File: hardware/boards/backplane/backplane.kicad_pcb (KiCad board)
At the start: 2 copper layers, 44 parts, among them J10 I2C_IN, J11 I2C_OUT, J12 LED_EXT_OUT, J13 FAN_3PIN, J2 SLOT_1, J3 SLOT_2, J4 SLOT_3, J5 SLOT_4, J6 SLOT_5, J7 SLOT_6, J8 LED_EXT_IN, Q1 Q_PMOS_GSD, Q2 Q_NPN_BEC, U1 TCA9548APWR, U2 WT32-ETH01

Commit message: Small tweaks to PCB/Schematic + 3d models
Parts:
- added D10: LOW_CAP_TVS, Diode_SMD:D_SOD-523, F.Cu at (65.5, 18.1)
- added D12: LOW_CAP_TVS, Diode_SMD:D_SOD-523, F.Cu at (69.1, 13.2)
- added D14: LOW_CAP_TVS, Diode_SMD:D_SOD-523, F.Cu at (69.1, 18.1)
- added D16: LOW_CAP_TVS, Diode_SMD:D_SOD-523, F.Cu at (72.7, 13.2)
- added D18: LOW_CAP_TVS, Diode_SMD:D_SOD-523, F.Cu at (72.7, 18.1)
- added D8: LOW_CAP_TVS, Diode_SMD:D_SOD-523, F.Cu at (65.5, 13.2)
- added H1: MountingHole_Pad, MountingHole:MountingHole_3.2mm_M3_Pad_Via, F.Cu at (-3.90, 0.50)
- added H2: MountingHole_Pad, MountingHole:MountingHole_3.2mm_M3_Pad_Via, F.Cu at (3.48, 11.4)
- added H3: MountingHole_Pad, MountingHole:MountingHole_3.2mm_M3_Pad_Via, F.Cu at (3.48, 19.4)
- added H4: MountingHole_Pad, MountingHole:MountingHole_3.2mm_M3_Pad_Via, F.Cu at (3.48, 27.3)
- added R11: 47R, Resistor_SMD:R_0603_1608Metric, F.Cu at (73.7, 3.27)
- added R13: 47R, Resistor_SMD:R_0603_1608Metric, F.Cu at (73.7, 8.29)
- added R3: 47R, Resistor_SMD:R_0603_1608Metric, F.Cu at (65.7, 3.27)
- added R5: 47R, Resistor_SMD:R_0603_1608Metric, F.Cu at (65.7, 8.29)
- added R7: 47R, Resistor_SMD:R_0603_1608Metric, F.Cu at (69.7, 3.27)
- added R9: 47R, Resistor_SMD:R_0603_1608Metric, F.Cu at (69.7, 8.29)
- J2: value SLOT_1 -> SLOT_4
- J3: value SLOT_2 -> SLOT_1
- J4: value SLOT_3 -> SLOT_2
- J5: value SLOT_4 -> SLOT_5
- J6: value SLOT_5 -> SLOT_6
- J7: value SLOT_6 -> SLOT_3
- moved J12 217.8 mm to (44.1, 14.0)
- moved J11 215.1 mm to (44.1, 1.79)
- moved D1 173.9 mm to (33.1, 2.81)
- moved D2 173.9 mm to (33.1, 9.43)
- moved D3 173.9 mm to (33.1, 16.1)
- moved D4 173.9 mm to (33.1, 22.7)
- moved D5 173.9 mm to (33.1, 29.3)
- moved D6 173.9 mm to (33.1, 35.9)
- moved J2 137.1 mm to (56.0, 2.62)
- moved J3 137.1 mm to (56.0, 8.88)
- moved J4 137.1 mm to (56.0, 15.1)
- moved J5 137.1 mm to (56.0, 21.4)
- moved J6 137.1 mm to (56.0, 27.6)
- moved J7 137.1 mm to (56.0, 33.9)
- moved R12 121.3 mm to (73.7, 5.78)
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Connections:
- J2 pad 3: SCL_SLOT_1_CONN -> Net-(D16-A1)
- J3 pad 3: SCL_SLOT_2_CONN -> Net-(D8-A1)
- J4 pad 3: SCL_SLOT_3_CONN -> Net-(D14-A1)
- J4 pad 4: Net-(D11-A1) -> Net-(D10-A1)
- J5 pad 3: SCL_SLOT_4_CONN -> Net-(D17-A1)
- J5 pad 4: Net-(D13-A1) -> Net-(D11-A1)
- J6 pad 3: SCL_SLOT_5_CONN -> Net-(D18-A1)
- J6 pad 4: Net-(D15-A1) -> Net-(D12-A1)
- J7 pad 3: SCL_SLOT_6_CONN -> Net-(D15-A1)
- J7 pad 4: Net-(D17-A1) -> Net-(D13-A1)
- R10 pad 1: SDA_SLOT_5 -> SCL_SLOT_3_CONN
- R12 pad 1: SDA_SLOT_6 -> SCL_SLOT_5_CONN
- R2 pad 1: SDA_SLOT_1 -> SDA_SLOT_4
- R4 pad 1: SDA_SLOT_2 -> SDA_SLOT_1
- R6 pad 1: SDA_SLOT_3 -> SDA_SLOT_5
- R8 pad 1: SDA_SLOT_4 -> SDA_SLOT_3

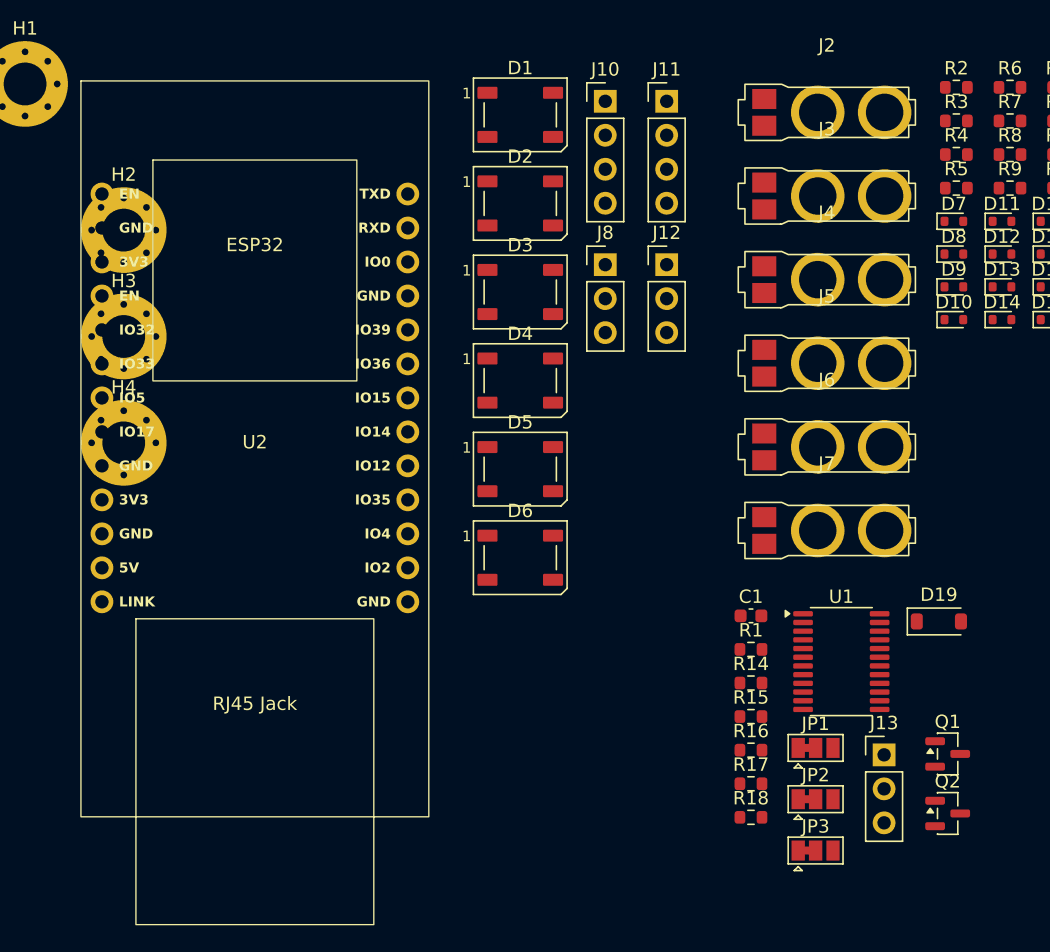
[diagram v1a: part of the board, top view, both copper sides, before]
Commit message: Split controller hardware from backplane
Add the central controller KiCad project for the WT32 and fan circuit, retain the I2C mux on the backplane, and update the system/interface documentation. Use C7519 arrays for interim slot I2C protection and record assembly-part alternatives.
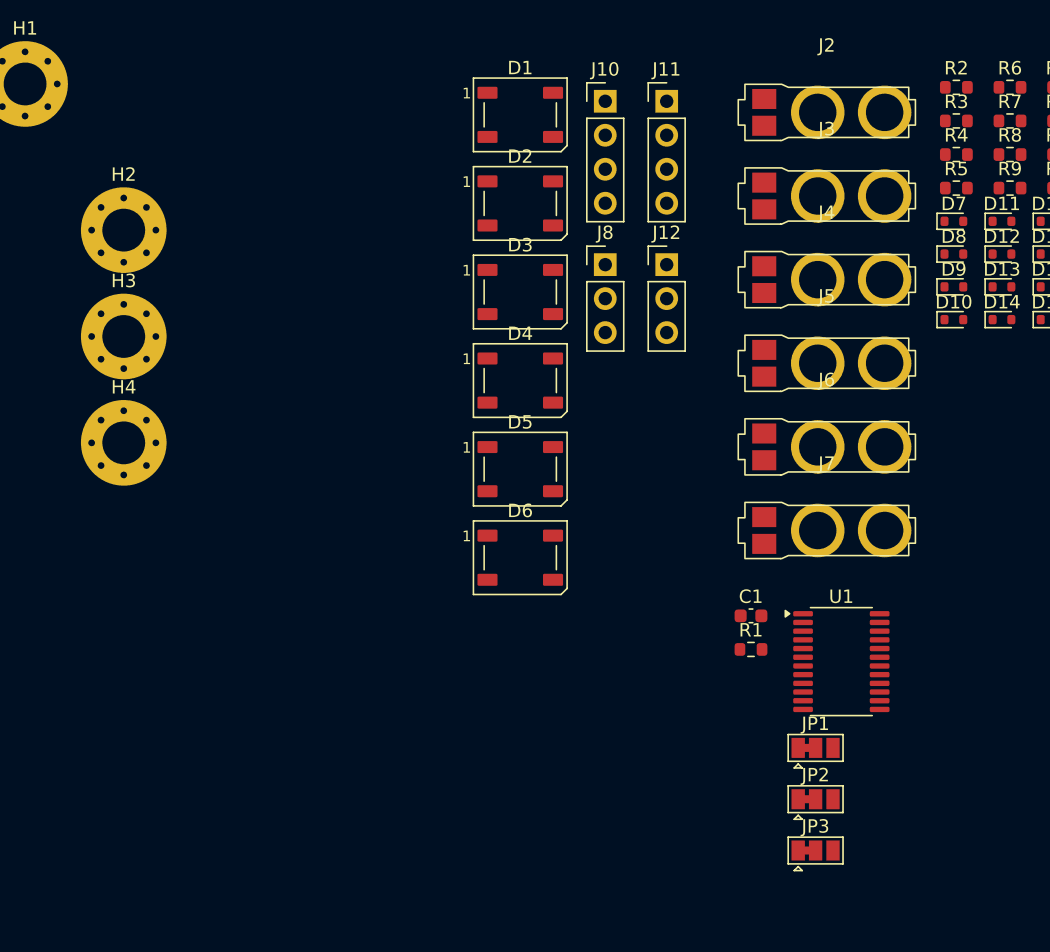
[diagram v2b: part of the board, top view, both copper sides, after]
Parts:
- removed D19: D_Schottky, Diode_SMD:D_SOD-123
- removed J13: FAN_3PIN, Connector_PinHeader_2.54mm:PinHeader_1x03_P2.54mm_Vertical
- removed Q1: Q_PMOS_GSD, Package_TO_SOT_SMD:SOT-23
- removed Q2: Q_NPN_BEC, Package_TO_SOT_SMD:SOT-23
- removed R14, R16: 100k, Resistor_SMD:R_0603_1608Metric
- removed R15: 4.7k, Resistor_SMD:R_0603_1608Metric
- removed R17: 10k, Resistor_SMD:R_0603_1608Metric
- removed R18: 1k, Resistor_SMD:R_0603_1608Metric
- removed U2: WT32-ETH01, WT32-ETH01:WT32-ETH01
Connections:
- net /I2C and Fan/TCA9548A_A0 renamed /I2C Mux/TCA9548A_A0
- net /I2C and Fan/TCA9548A_A1 renamed /I2C Mux/TCA9548A_A1
- net /I2C and Fan/TCA9548A_A2 renamed /I2C Mux/TCA9548A_A2
- net Net-(D1-DIN) renamed /Slots and LEDs/LED_DATA_IN
- J10 pad 4: +5V -> +3V3
- J11 pad 4: +5V -> +3V3

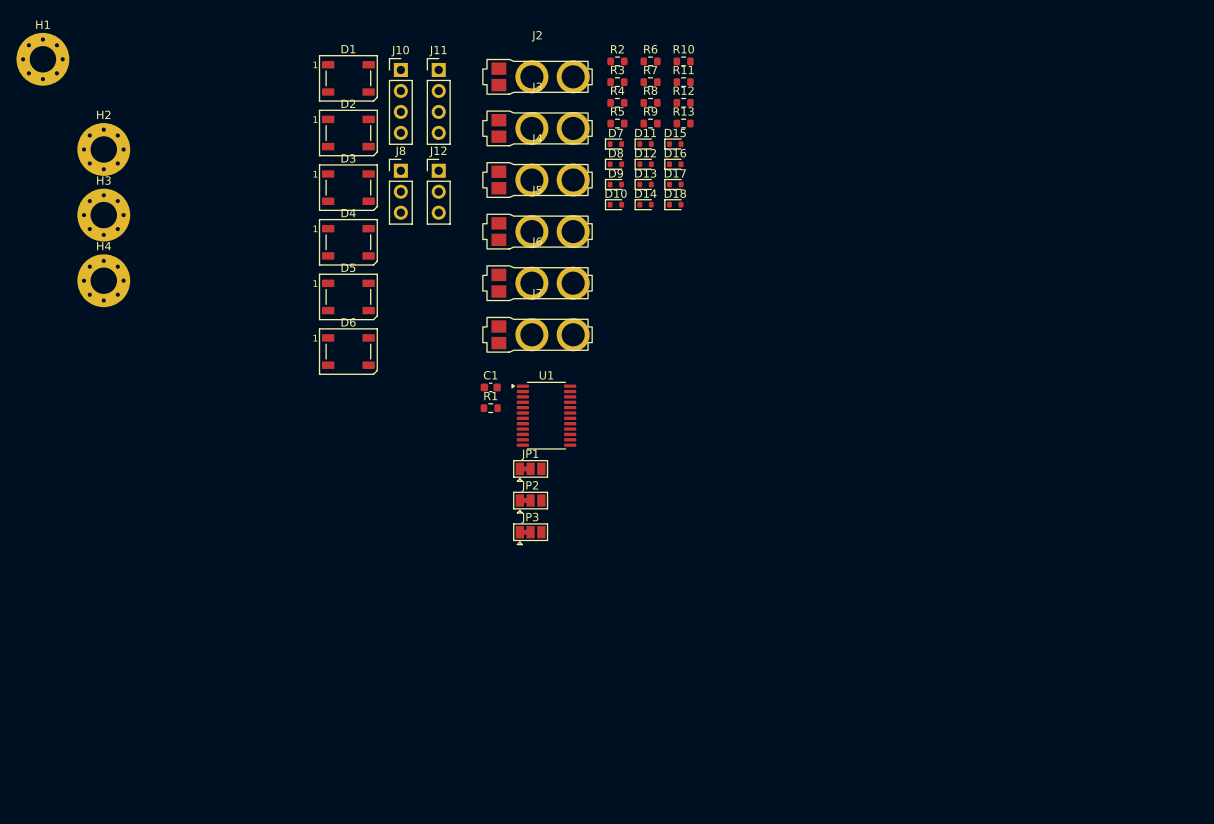
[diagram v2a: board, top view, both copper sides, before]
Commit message: Add adjustable DC-DC module to backplane
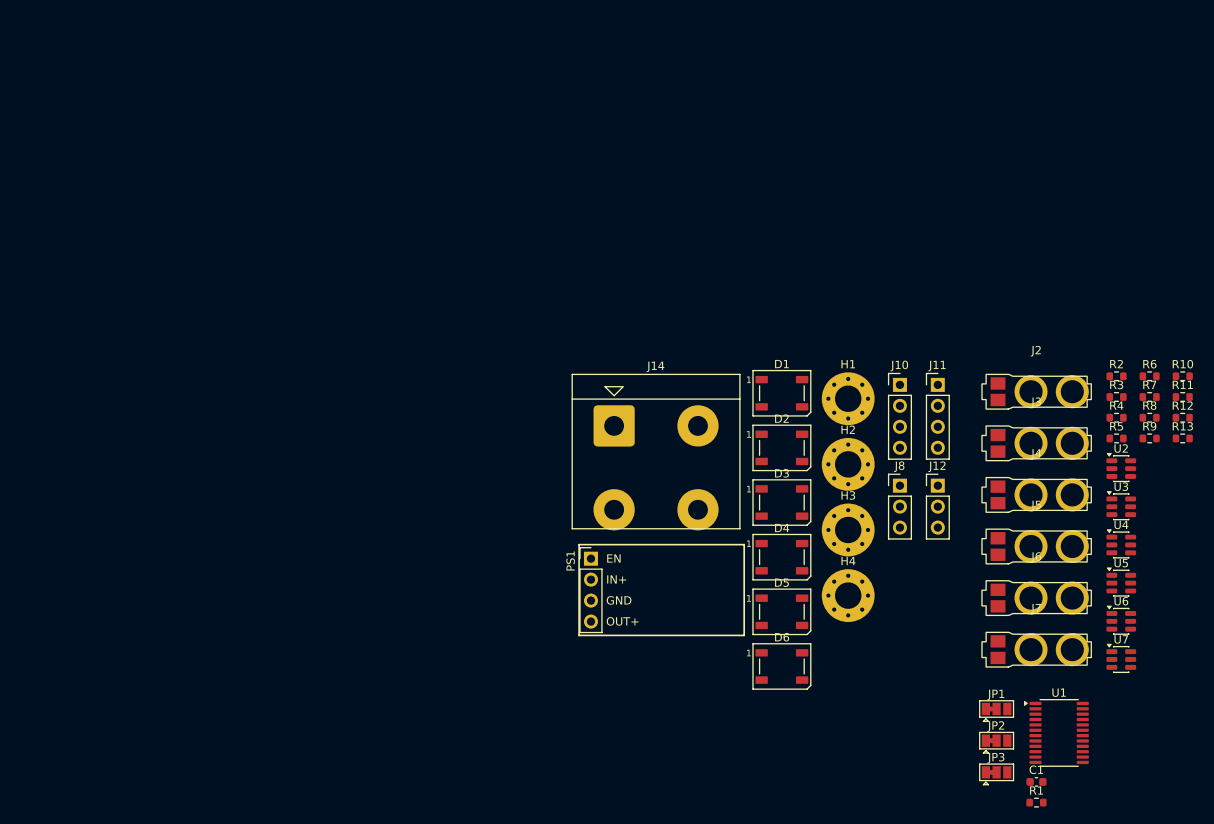
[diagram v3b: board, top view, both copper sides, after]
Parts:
- removed D10, D11, D12, D13, D14, D15, D16, D17, D18, D7, D8, D9: LOW_CAP_TVS, Diode_SMD:D_SOD-523
- added J14: DC_IN, mini-rack-power:DEGSON_DG135T-10.16-02P, F.Cu at (65.3, 44.9)
- added PS1: Adjustable_DC2DC, mini-rack-power:Adjustable_DC2DC, F.Cu at (62.5, 61.0)
- added U2: USBLC6-2SC6, Package_TO_SOT_SMD:SOT-23-6, F.Cu at (126.7, 50.1)
- added U3: USBLC6-2SC6, Package_TO_SOT_SMD:SOT-23-6, F.Cu at (126.7, 54.7)
- added U4: USBLC6-2SC6, Package_TO_SOT_SMD:SOT-23-6, F.Cu at (126.7, 59.3)
- added U5: USBLC6-2SC6, Package_TO_SOT_SMD:SOT-23-6, F.Cu at (126.7, 64.0)
- added U6: USBLC6-2SC6, Package_TO_SOT_SMD:SOT-23-6, F.Cu at (126.7, 68.6)
- added U7: USBLC6-2SC6, Package_TO_SOT_SMD:SOT-23-6, F.Cu at (126.7, 73.2)
- moved H1 105.9 mm to (93.7, 41.6)
- moved H2 97.9 mm to (93.7, 49.6)
- moved H3 97.9 mm to (93.7, 57.5)
- moved H4 97.9 mm to (93.7, 65.5)
- moved R1 81.6 mm to (116.5, 90.6)
- moved C1 81.6 mm to (116.5, 88.0)
- moved U1 73.0 mm to (119.2, 82.1)
- moved J10 71.5 mm to (99.9, 39.9)
- moved J6 71.5 mm to (116.5, 65.8)
- moved J7 71.5 mm to (116.5, 72.0)
- moved J8 71.5 mm to (99.9, 52.2)
- moved R10 71.5 mm to (134.2, 38.9)
- moved R11 71.5 mm to (134.2, 41.4)
- moved R12 71.5 mm to (134.2, 43.9)
- moved R13 71.5 mm to (134.2, 46.4)
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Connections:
- J2 pad 3: Net-(D16-A1) -> Net-(J2-Pin_3)
- J2 pad 4: Net-(D7-A1) -> Net-(J2-Pin_4)
- J3 pad 3: Net-(D8-A1) -> Net-(J3-Pin_3)
- J3 pad 4: Net-(D9-A1) -> Net-(J3-Pin_4)
- J4 pad 3: Net-(D14-A1) -> Net-(J4-Pin_3)
- J4 pad 4: Net-(D10-A1) -> Net-(J4-Pin_4)
- J5 pad 3: Net-(D17-A1) -> Net-(J5-Pin_3)
- J5 pad 4: Net-(D11-A1) -> Net-(J5-Pin_4)
- J6 pad 3: Net-(D18-A1) -> Net-(J6-Pin_3)
- J6 pad 4: Net-(D12-A1) -> Net-(J6-Pin_4)
- J7 pad 3: Net-(D15-A1) -> Net-(J7-Pin_3)
- J7 pad 4: Net-(D13-A1) -> Net-(J7-Pin_4)
- R10 pad 1: SCL_SLOT_3_CONN -> SCL_SLOT_3
- R10 pad 2: Net-(D15-A1) -> Net-(R10-Pad2)
- R11 pad 1: SCL_SLOT_4_CONN -> SCL_SLOT_4
- R11 pad 2: Net-(D16-A1) -> Net-(R11-Pad2)
- R12 pad 1: SCL_SLOT_5_CONN -> SCL_SLOT_5
- R12 pad 2: Net-(D17-A1) -> Net-(R12-Pad2)
- R13 pad 1: SCL_SLOT_6_CONN -> SCL_SLOT_6
- R13 pad 2: Net-(D18-A1) -> Net-(R13-Pad2)
- R2 pad 2: Net-(D7-A1) -> Net-(R2-Pad2)
- R3 pad 1: SCL_SLOT_1_CONN -> SCL_SLOT_1
- R3 pad 2: Net-(D8-A1) -> Net-(R3-Pad2)
- R4 pad 2: Net-(D9-A1) -> Net-(R4-Pad2)
- R5 pad 2: Net-(D10-A1) -> Net-(R5-Pad2)
- R6 pad 2: Net-(D11-A1) -> Net-(R6-Pad2)
- R7 pad 2: Net-(D12-A1) -> Net-(R7-Pad2)
- R8 pad 2: Net-(D13-A1) -> Net-(R8-Pad2)
- R9 pad 1: SCL_SLOT_2_CONN -> SCL_SLOT_2
- R9 pad 2: Net-(D14-A1) -> Net-(R9-Pad2)

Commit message: Save initial backplane placement work
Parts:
- added J1: SPARE_I2C, Connector_PinHeader_2.54mm:PinHeader_1x04_P2.54mm_Vertical, F.Cu at (-26.1, 46.2)
- moved C1 136.8 mm to (-16.1, 54.5)
- moved JP1 136.8 mm to (-20.9, 45.7)
- moved JP2 136.8 mm to (-20.9, 49.5)
- moved JP3 136.8 mm to (-20.9, 53.4)
- moved R1 136.8 mm to (-16.1, 57.0)
- moved U1 136.8 mm to (-13.4, 48.6)
- moved H1 129.1 mm to (-32.0, 71.2)
- moved H2 129.1 mm to (-32.0, 79.2)
- moved H3 129.1 mm to (-32.0, 87.1)
- moved H4 129.1 mm to (-32.0, 95.0)
- moved J10 121.1 mm to (-18.8, 16.5)
- moved J11 121.1 mm to (-14.2, 16.5)
- moved J12 121.1 mm to (-14.2, 28.7)
- moved J8 121.1 mm to (-18.8, 28.7)
- moved PS1 92.9 mm to (-25.5, 90.7)
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
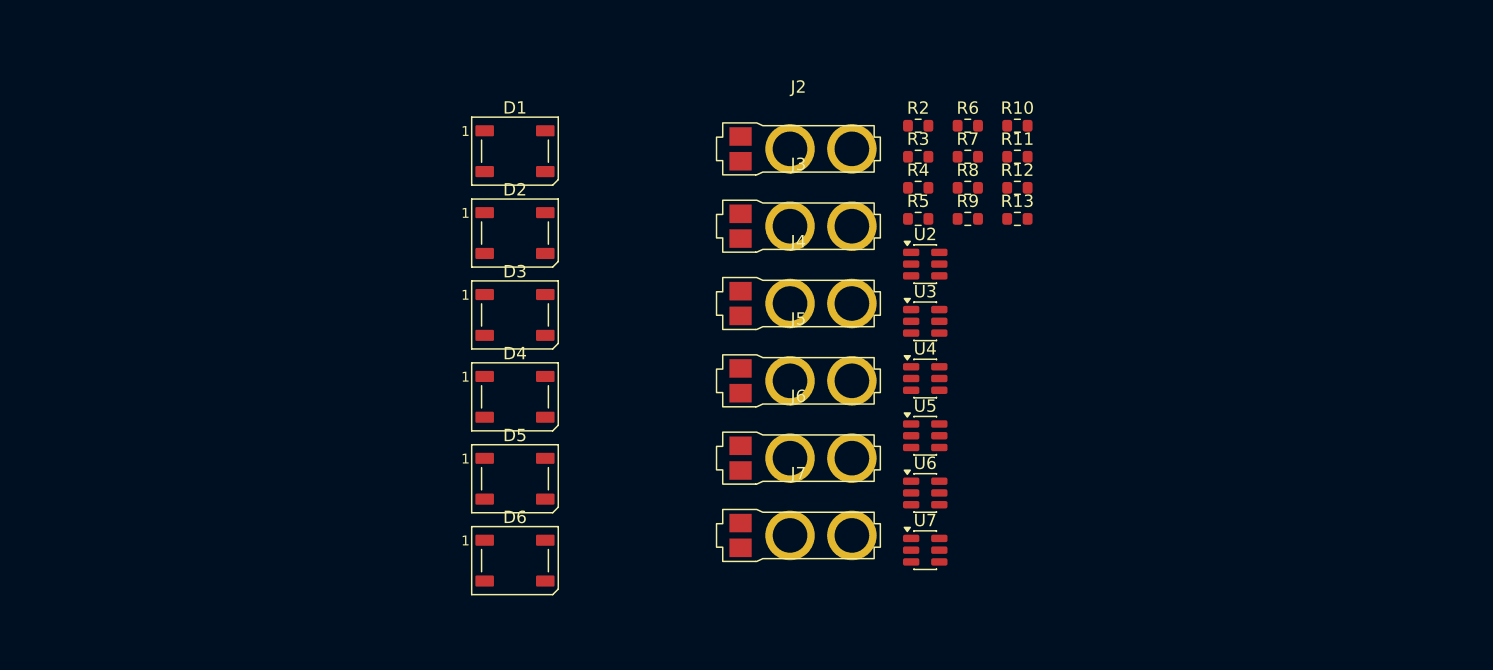
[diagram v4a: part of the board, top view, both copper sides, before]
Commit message: Arrange backplane slot connector groups
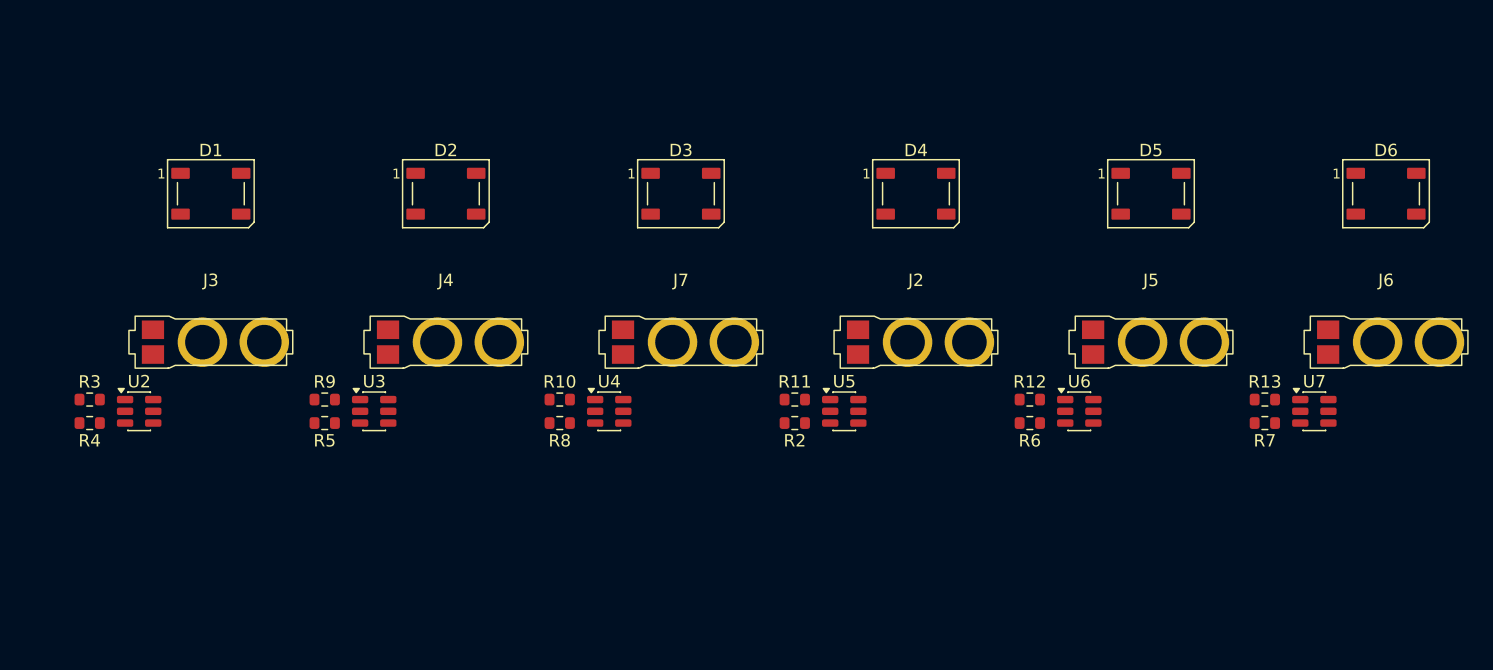
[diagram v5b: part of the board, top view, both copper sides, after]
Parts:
- moved D6 76.4 mm to (163.8, 52.9)
- moved R3 69.8 mm to (59.0, 69.5)
- moved R4 69.6 mm to (59.0, 71.5)
- moved U2 64.6 mm to (63.0, 70.5)
- moved D5 56.3 mm to (144.8, 52.9)
- moved R9 54.0 mm to (78.0, 69.5)
- moved R5 50.7 mm to (78.0, 71.5)
- moved J3 48.4 mm to (68.8, 64.9)
- moved J6 48.4 mm to (163.8, 64.9)
- moved U3 45.1 mm to (82.0, 70.5)
- moved R10 43.1 mm to (97.0, 69.5)
- moved R8 38.1 mm to (97.0, 71.5)
- moved D4 36.3 mm to (125.8, 52.9)
- moved U7 33.4 mm to (158.0, 70.5)
- moved R7 32.2 mm to (154.0, 71.5)
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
